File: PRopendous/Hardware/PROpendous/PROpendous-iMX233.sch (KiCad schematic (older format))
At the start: 17 parts, among them IC1 i.MX233, SW1 POWER, X1 24MHz

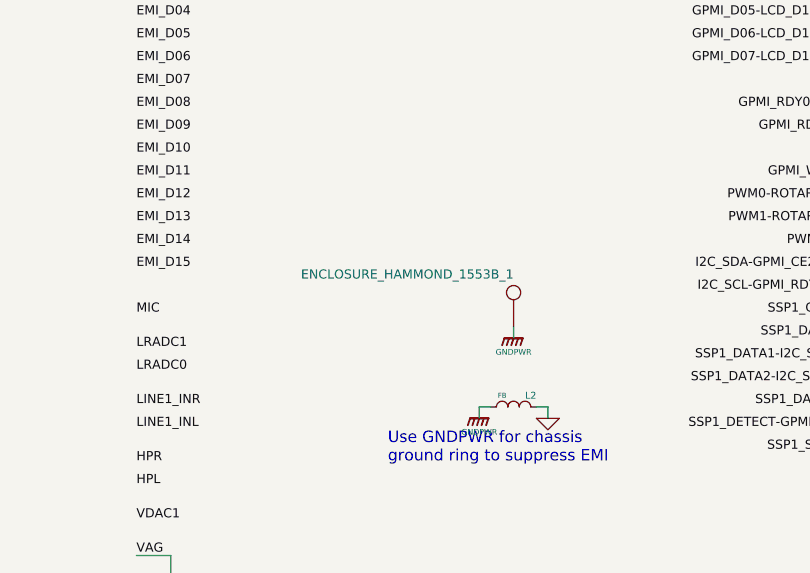
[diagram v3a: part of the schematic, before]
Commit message: Minor update to schematic.  Removed USB Power switch and added some notes.
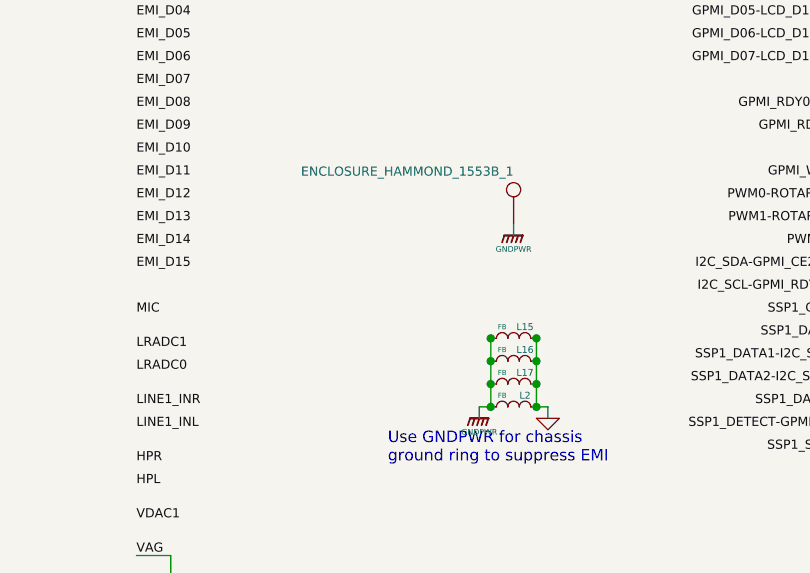
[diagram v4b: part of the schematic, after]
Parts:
- added L15, L16, L17: FB, symbol L_MINI
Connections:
- wire segments 50 -> 52
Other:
- moved on the sheet: ENCLOSURE_HAMMOND_1553B_1
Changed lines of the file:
@@
-EESchema Schematic File Version 2  date 19/04/2010 19:59:31
+EESchema Schematic File Version 2  date 21/04/2010 18:06:05
 LIBS:opendous
 LIBS:device
@@
 Sheet 2 8
 Title "PROpendous"
-Date "19 apr 2010"
+Date "21 apr 2010"
 Rev "1.0"
 Comp "Opendous Inc. (www.opendous.org)"
@@
 Comment4 "www.PROpendous.org"
 $EndDescr
+Connection ~ 7250 5750
+Connection ~ 7450 5750
+Connection ~ 7450 6050
+Connection ~ 7250 6050
+Connection ~ 7450 5850
+Wire Wire Line
+	7450 5750 7450 6050
+Connection ~ 7250 5950
+Wire Wire Line
+	6450 7500 6450 7450
+Wire Wire Line
+	6450 7450 6400 7450
+Wire Wire Line
+	6200 7450 6150 7450
+Wire Wire Line
+	6150 7450 6150 7500
+Wire Wire Line
+	7200 6100 7200 6050
+Wire Wire Line
+	7200 6050 7250 6050
+Connection ~ 5100 950
+Wire Wire Line
+	5100 700  5100 950
+Connection ~ 4700 950
+Wire Wire Line
+	4900 950  4600 950
+Wire Wire Line
+	4550 7350 4550 7250
+Connection ~ 4150 7250
+Wire Wire Line
+	3650 7250 4250 7250
+Connection ~ 3900 7250
+Connection ~ 1300 1500
+Wire Wire Line
+	1300 1700 1300 1500
+Connection ~ 1100 1500
+Wire Wire Line
+	650  1350 650  1500
+Connection ~ 1200 2050
+Wire Wire Line
+	1100 2050 1300 2050
+Wire Wire Line
+	1300 2050 1300 1900
+Wire Wire Line
+	650  1500 750  1500
+Wire Wire Line
+	650  1850 650  1800
+Wire Wire Line
+	5850 7000 5850 7100
+Connection ~ 1900 900
+Wire Wire Line
+	2200 1200 1900 1200
+Wire Wire Line
+	1900 1200 1900 750
+Wire Wire Line
+	1300 550  1900 550
+Wire Wire Line
+	4300 700  4300 950
+Connection ~ 3800 950
+Wire Wire Line
+	3700 950  3900 950
+Connection ~ 4100 950
+Wire Wire Line
+	4100 700  4100 950
+Wire Wire Line
+	3400 900  3400 950
+Wire Wire Line
+	3050 950  3050 700
+Wire Wire Line
+	2800 700  2800 950
+Wire Wire Line
+	2800 950  2900 950
+Connection ~ 2800 950
+Wire Wire Line
+	3200 900  3200 950
+Wire Wire Line
+	4050 950  4150 950
+Wire Wire Line
+	3800 700  3800 950
+Wire Wire Line
+	3550 950  3550 700
+Wire Wire Line
+	4450 850  4450 950
+Wire Wire Line
+	1600 600  1600 550
+Connection ~ 1600 550
+Wire Wire Line
+	1300 750  1300 1300
+Wire Wire Line
+	1300 1300 2200 1300
+Connection ~ 1300 900
+Wire Wire Line
+	5700 6700 5850 6700
+Wire Wire Line
+	5850 6700 5850 6800
+Wire Wire Line
+	650  2100 650  2050
+Wire Wire Line
+	1200 2100 1200 2050
+Wire Wire Line
+	1100 1850 1100 1750
+Wire Wire Line
+	1550 1500 2200 1500
+Wire Wire Line
+	1350 1500 1050 1500
+Wire Wire Line
+	1100 1450 1100 1550
+Wire Wire Line
+	1100 1250 1100 1200
+Connection ~ 3800 7250
+Connection ~ 4000 7250
+Wire Wire Line
+	3950 7250 3950 7350
+Connection ~ 3950 7250
+Wire Wire Line
+	7350 5300 7350 5250
+Wire Wire Line
+	5150 950  5050 950
+Connection ~ 4800 950
+Wire Wire Line
+	4750 950  4750 700
+Connection ~ 4750 950
+Wire Wire Line
+	7450 6050 7500 6050
+Wire Wire Line
+	7500 6050 7500 6100
+Wire Wire Line
+	7250 6050 7250 5750
+Connection ~ 7250 5850
+Connection ~ 7450 5950
+$Comp
+L L_MINI L15
+U 1 1 4BCED957
+P 7350 5750
+F 0 "L15" H 7300 5700 30  0000 C CNN
+F 1 "FB" H 7400 5700 22  0000 C CNN
+	1    7350 5750
+	-1   0    0    1
+$EndComp
+$Comp
+L L_MINI L16
+U 1 1 4BCED953
+P 7350 5850
+F 0 "L16" H 7300 5800 30  0000 C CNN
+F 1 "FB" H 7400 5800 22  0000 C CNN
+	1    7350 5850
+	-1   0    0    1
+$EndComp
+$Comp
+L L_MINI L17
+U 1 1 4BCED94E
+P 7350 5950
+F 0 "L17" H 7300 5900 30  0000 C CNN
+F 1 "FB" H 7400 5900 22  0000 C CNN
+	1    7350 5950
+	-1   0    0    1
+$EndComp
 $Comp
 L L_MINI L14
@@
 	1    0    0    -1
 $EndComp
-Wire Wire Line
-	6450 7500 6450 7450
-Wire Wire Line
-	6450 7450 6400 7450
-Wire Wire Line
-	6200 7450 6150 7450
-Wire Wire Line
-	6150 7450 6150 7500
 $Comp
 L GND1 #PWR02
@@
 Text Notes 6800 6300 0    50   ~ 0
 Use GNDPWR for chassis\nground ring to suppress EMI
-Wire Wire Line
-	7200 6100 7200 6050
-Wire Wire Line
-	7200 6050 7250 6050
-Connection ~ 5100 950
-Wire Wire Line
-	5100 700  5100 950
-Connection ~ 4700 950
-Wire Wire Line
-	4900 950  4600 950
-Wire Wire Line
-	4550 7350 4550 7250
-Connection ~ 4150 7250
-Wire Wire Line
-	3650 7250 4250 7250
-Connection ~ 3900 7250
-Connection ~ 1300 1500
-Wire Wire Line
-	1300 1700 1300 1500
-Connection ~ 1100 1500
-Wire Wire Line
-	650  1350 650  1500
-Connection ~ 1200 2050
-Wire Wire Line
-	1100 2050 1300 2050
-Wire Wire Line
-	1300 2050 1300 1900
-Wire Wire Line
-	650  1500 750  1500
-Wire Wire Line
-	650  1850 650  1800
-Wire Wire Line
-	5850 7000 5850 7100
-Connection ~ 1900 900
-Wire Wire Line
-	2200 1200 1900 1200
-Wire Wire Line
-	1900 1200 1900 750
-Wire Wire Line
-	1300 550  1900 550
-Wire Wire Line
-	4300 700  4300 950
-Connection ~ 3800 950
-Wire Wire Line
-	3700 950  3900 950
-Connection ~ 4100 950
-Wire Wire Line
-	4100 700  4100 950
-Wire Wire Line
-	3400 900  3400 950
-Wire Wire Line
-	3050 950  3050 700
-Wire Wire Line
-	2800 700  2800 950
-Wire Wire Line
-	2800 950  2900 950
-Connection ~ 2800 950
-Wire Wire Line
-	3200 900  3200 950
-Wire Wire Line
-	4050 950  4150 950
-Wire Wire Line
-	3800 700  3800 950
-Wire Wire Line
-	3550 950  3550 700
-Wire Wire Line
-	4450 850  4450 950
-Wire Wire Line
-	1600 600  1600 550
-Connection ~ 1600 550
-Wire Wire Line
-	1300 750  1300 1300
-Wire Wire Line
-	1300 1300 2200 1300
-Connection ~ 1300 900
-Wire Wire Line
-	5700 6700 5850 6700
-Wire Wire Line
-	5850 6700 5850 6800
-Wire Wire Line
-	650  2100 650  2050
-Wire Wire Line
-	1200 2100 1200 2050
-Wire Wire Line
-	1100 1850 1100 1750
-Wire Wire Line
-	1550 1500 2200 1500
-Wire Wire Line
-	1350 1500 1050 1500
-Wire Wire Line
-	1100 1450 1100 1550
-Wire Wire Line
-	1100 1250 1100 1200
-Connection ~ 3800 7250
-Connection ~ 4000 7250
-Wire Wire Line
-	3950 7250 3950 7350
-Connection ~ 3950 7250
-Wire Wire Line
-	7350 5750 7350 5700
-Wire Wire Line
-	5150 950  5050 950
-Connection ~ 4800 950
-Wire Wire Line
-	4750 950  4750 700
-Connection ~ 4750 950
-Wire Wire Line
-	7450 6050 7500 6050
-Wire Wire Line
-	7500 6050 7500 6100
 $Comp
 L GND #PWR03
@@
 U 1 1 4BCC48AC
 P 7350 6050
-F 0 "L2" H 7275 6000 30  0000 C CNN
+F 0 "L2" H 7300 6000 30  0000 C CNN
 F 1 "FB" H 7400 6000 22  0000 C CNN
 	1    7350 6050
@@
 L GNDPWR #PWR06
 U 1 1 4BBD1ABB
-P 7350 5750
-F 0 "#PWR06" H 7350 5800 40  0001 C CNN
-F 1 "GNDPWR" H 7350 5690 25  0000 C CNN
-	1    7350 5750
+P 7350 5300
+F 0 "#PWR06" H 7350 5350 40  0001 C CNN
+F 1 "GNDPWR" H 7350 5240 25  0000 C CNN
+	1    7350 5300
 	1    0    0    -1
 $EndComp
@@
 L CONN_1 ENCLOSURE_HAMMOND_1553B_1
 U 1 1 4BBD1A8C
-P 7350 5550
-F 0 "ENCLOSURE_HAMMOND_1553B_1" V 7430 5550 40  0000 L CNN
-F 1 "CONN_1" H 7350 5605 30  0001 C CNN
-	1    7350 5550
+P 7350 5100
+F 0 "ENCLOSURE_HAMMOND_1553B_1" V 7430 5100 40  0000 L CNN
+F 1 "CONN_1" H 7350 5155 30  0001 C CNN
+	1    7350 5100
 	0    -1   -1   0
 $EndComp

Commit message: Updated PROpendous Project.  PCB layout is nearing completion.
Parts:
- L14: value FB -> Trace
- renumbered ENCLOSURE_HAMMOND_1553B_1 to ENCLOSURE_HAMMOND_1553B_BAT_1
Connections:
- net labels added: VDD4P2
- net labels removed: VDD4V2
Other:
- note added: "1A Maximum"
- note added: "Bourns"
- note added: "L14 is a PCB trace"
- note added: "SRR4028-150Y"
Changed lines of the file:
@@
-EESchema Schematic File Version 2  date 21/04/2010 18:06:05
+EESchema Schematic File Version 2  date 24/04/2010 02:27:16
 LIBS:opendous
 LIBS:device
@@
 Sheet 2 8
 Title "PROpendous"
-Date "21 apr 2010"
+Date "24 apr 2010"
 Rev "1.0"
 Comp "Opendous Inc. (www.opendous.org)"
@@
 Comment4 "www.PROpendous.org"
 $EndDescr
+Text Notes 3200 815  0    22   ~ 0
+1A Maximum
+Text Notes 3240 725  0    25   ~ 0
+Bourns
+$Comp
+L IMX233 IC1
+U 1 1 4BD121E5
+P 3950 4100
+F 0 "IC1" H 2450 1050 60  0000 C CNN
+F 1 "i.MX233" H 2525 7150 60  0000 C CNN
+	1    3950 4100
+	1    0    0    -1
+$EndComp
+Text Notes 3150 775  0    27   ~ 0
+SRR4028-150Y
+Text Notes 6000 7675 0    40   ~ 0
+L14 is a PCB trace
 Connection ~ 7250 5750
 Connection ~ 7450 5750
@@
 P 6300 7450
 F 0 "L14" H 6225 7400 30  0000 C CNN
-F 1 "FB" H 6350 7400 22  0000 C CNN
+F 1 "Trace" H 6350 7400 22  0000 C CNN
 	1    6300 7450
 	-1   0    0    1
@@
 F 1 "GND1" H 6150 7430 30  0000 C CNN
 	1    6150 7500
-	1    0    0    -1
-$EndComp
-$Comp
-L IMX233 IC1
-U 1 1 4BCC6F47
-P 3950 4100
-F 0 "IC1" H 2450 1050 60  0000 C CNN
-F 1 "i.MX233" H 2525 7150 60  0000 C CNN
-	1    3950 4100
 	1    0    0    -1
 $EndComp
@@
 $EndComp
 $Comp
-L CONN_1 ENCLOSURE_HAMMOND_1553B_1
+L CONN_1 ENCLOSURE_HAMMOND_1553B_BAT_1
 U 1 1 4BBD1A8C
 P 7350 5100
-F 0 "ENCLOSURE_HAMMOND_1553B_1" V 7430 5100 40  0000 L CNN
+F 0 "ENCLOSURE_HAMMOND_1553B_BAT_1" V 7430 5100 40  0000 L CNN
 F 1 "CONN_1" H 7350 5155 30  0001 C CNN
 	1    7350 5100
@@
 $EndComp
 $Comp
-L VDD4V2 #PWR021
+L VDD4P2 #PWR021
 U 1 1 4BBCC950
 P 3050 700
 F 0 "#PWR021" H 3050 800 30  0001 C CNN
-F 1 "VDD4V2" H 3050 800 30  0000 C CNN
+F 1 "VDD4P2" H 3050 800 30  0000 C CNN
 	1    3050 700
 	1    0    0    -1

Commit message: Updated layout.
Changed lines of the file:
@@
-EESchema Schematic File Version 2  date 24/04/2010 02:27:16
+EESchema Schematic File Version 2  date 25/04/2010 06:05:23
 LIBS:opendous
 LIBS:device
@@
 Sheet 2 8
 Title "PROpendous"
-Date "24 apr 2010"
+Date "25 apr 2010"
 Rev "1.0"
 Comp "Opendous Inc. (www.opendous.org)"
@@
 Comment4 "www.PROpendous.org"
 $EndDescr
+$Comp
+L IMX233 IC1
+U 1 1 4BD3DE42
+P 3950 4100
+F 0 "IC1" H 2450 1050 60  0000 C CNN
+F 1 "i.MX233" H 2525 7150 60  0000 C CNN
+	1    3950 4100
+	1    0    0    -1
+$EndComp
 Text Notes 3200 815  0    22   ~ 0
 1A Maximum
 Text Notes 3240 725  0    25   ~ 0
 Bourns
-$Comp
-L IMX233 IC1
-U 1 1 4BD121E5
-P 3950 4100
-F 0 "IC1" H 2450 1050 60  0000 C CNN
-F 1 "i.MX233" H 2525 7150 60  0000 C CNN
-	1    3950 4100
-	1    0    0    -1
-$EndComp
 Text Notes 3150 775  0    27   ~ 0
 SRR4028-150Y
@@
 Text Label 5700 4550 0    40   ~ 0
 EMI_D06
-Text Label 5700 3500 0    40   ~ 0
+Text Label 5700 3700 0    40   ~ 0
 EMI_DQS0
-Text Label 5700 2950 0    40   ~ 0
+Text Label 5700 3150 0    40   ~ 0
 EMI_CKE
 Text Label 5700 2000 0    40   ~ 0
@@
 Text Label 5700 4450 0    40   ~ 0
 EMI_D05
-Text Label 5700 3800 0    40   ~ 0
+Text Label 5700 3050 0    40   ~ 0
 EMI_WEn
 Text Label 5700 2100 0    40   ~ 0
@@
 Text Label 5700 4350 0    40   ~ 0
 EMI_D04
-Text Label 5700 3150 0    40   ~ 0
+Text Label 5700 3400 0    40   ~ 0
 EMI_CLKn
 Text Label 5700 1200 0    40   ~ 0
@@
 Text Label 5700 2200 0    40   ~ 0
 EMI_A10
-Text Label 5700 3400 0    40   ~ 0
+Text Label 5700 3600 0    40   ~ 0
 EMI_DQM1
+Text Label 5700 3500 0    40   ~ 0
+EMI_DQM0
 Text Label 5700 3300 0    40   ~ 0
-EMI_DQM0
-Text Label 5700 3050 0    40   ~ 0
 EMI_CLK
 Text Label 5700 1300 0    40   ~ 0
@@
 Text Label 5700 1500 0    40   ~ 0
 EMI_A03
-Text Label 5700 2850 0    40   ~ 0
+Text Label 5700 2950 0    40   ~ 0
 EMI_CE0n
 Text Label 5700 4050 0    40   ~ 0
@@
 Text Label 5700 1600 0    40   ~ 0
 EMI_A04
-Text Label 5700 3700 0    40   ~ 0
+Text Label 5700 2850 0    40   ~ 0
 EMI_RASn
 Text Label 5700 4850 0    40   ~ 0
@@
 Text Label 5700 4650 0    40   ~ 0
 EMI_D07
-Text Label 5700 3600 0    40   ~ 0
+Text Label 5700 3800 0    40   ~ 0
 EMI_DQS1
 Text Label 2200 5900 2    40   ~ 0

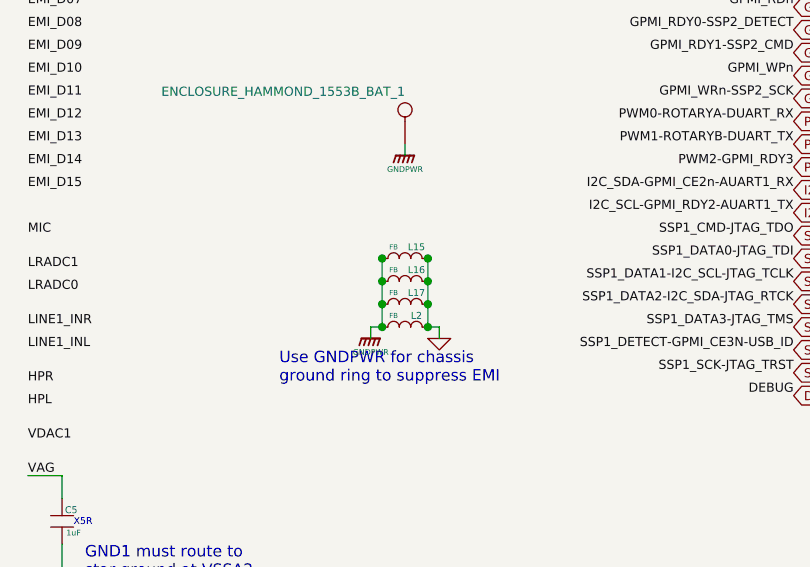
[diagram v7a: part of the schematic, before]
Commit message: First revision of i.MX233-based PROpendous board is complete.
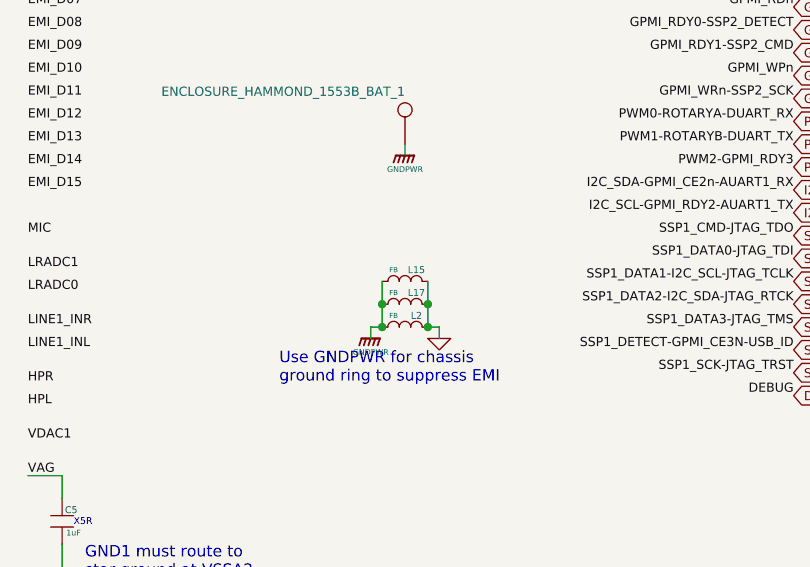
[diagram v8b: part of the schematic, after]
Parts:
- removed L16: FB, symbol L_MINI
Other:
- moved on the sheet: L15
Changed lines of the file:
@@
-EESchema Schematic File Version 2  date 25/04/2010 07:03:32
+EESchema Schematic File Version 2  date 26/04/2010 13:13:01
 LIBS:opendous
 LIBS:device
@@
 Sheet 2 8
 Title "PROpendous"
-Date "25 apr 2010"
+Date "26 apr 2010"
 Rev "1.0"
 Comp "Opendous Inc. (www.opendous.org)"
@@
 Comment4 "www.PROpendous.org"
 $EndDescr
-$Comp
-L IMX233 IC1
-U 1 1 4BD3DE42
-P 3950 4100
-F 0 "IC1" H 2450 1050 60  0000 C CNN
-F 1 "i.MX233" H 2525 7150 60  0000 C CNN
-	1    3950 4100
-	1    0    0    -1
-$EndComp
-Text Notes 3200 815  0    22   ~ 0
-1A Maximum
-Text Notes 3240 725  0    25   ~ 0
-Bourns
-Text Notes 3150 775  0    27   ~ 0
-SRR4028-150Y
-Text Notes 6000 7675 0    40   ~ 0
-L14 is a PCB trace
-Connection ~ 7250 5750
-Connection ~ 7450 5750
 Connection ~ 7450 6050
 Connection ~ 7250 6050
-Connection ~ 7450 5850
 Wire Wire Line
-	7450 5750 7450 6050
+	7450 5850 7450 6050
 Connection ~ 7250 5950
 Wire Wire Line
@@
 	7500 6050 7500 6100
 Wire Wire Line
-	7250 6050 7250 5750
-Connection ~ 7250 5850
+	7250 6050 7250 5850
 Connection ~ 7450 5950
+$Comp
+L IMX233 IC1
+U 1 1 4BD3DE42
+P 3950 4100
+F 0 "IC1" H 2450 1050 60  0000 C CNN
+F 1 "i.MX233" H 2525 7150 60  0000 C CNN
+	1    3950 4100
+	1    0    0    -1
+$EndComp
+Text Notes 3200 815  0    22   ~ 0
+1A Maximum
+Text Notes 3240 725  0    25   ~ 0
+Bourns
+Text Notes 3150 775  0    27   ~ 0
+SRR4028-150Y
+Text Notes 6000 7675 0    40   ~ 0
+L14 is a PCB trace
 $Comp
 L L_MINI L15
 U 1 1 4BCED957
-P 7350 5750
-F 0 "L15" H 7300 5700 30  0000 C CNN
-F 1 "FB" H 7400 5700 22  0000 C CNN
-	1    7350 5750
-	-1   0    0    1
-$EndComp
-$Comp
-L L_MINI L16
-U 1 1 4BCED953
 P 7350 5850
-F 0 "L16" H 7300 5800 30  0000 C CNN
+F 0 "L15" H 7300 5800 30  0000 C CNN
 F 1 "FB" H 7400 5800 22  0000 C CNN
 	1    7350 5850
